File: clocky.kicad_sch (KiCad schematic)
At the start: 78 parts, among them J1 Bot 50 pin, J2 Bot 40 pin, J3 Top 50 pin, J4 Top 40 pin, J5 Power, J51 Program, J6 JST_PH, J7 Boot, Q1 AO3401A, U1 HEF4094B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

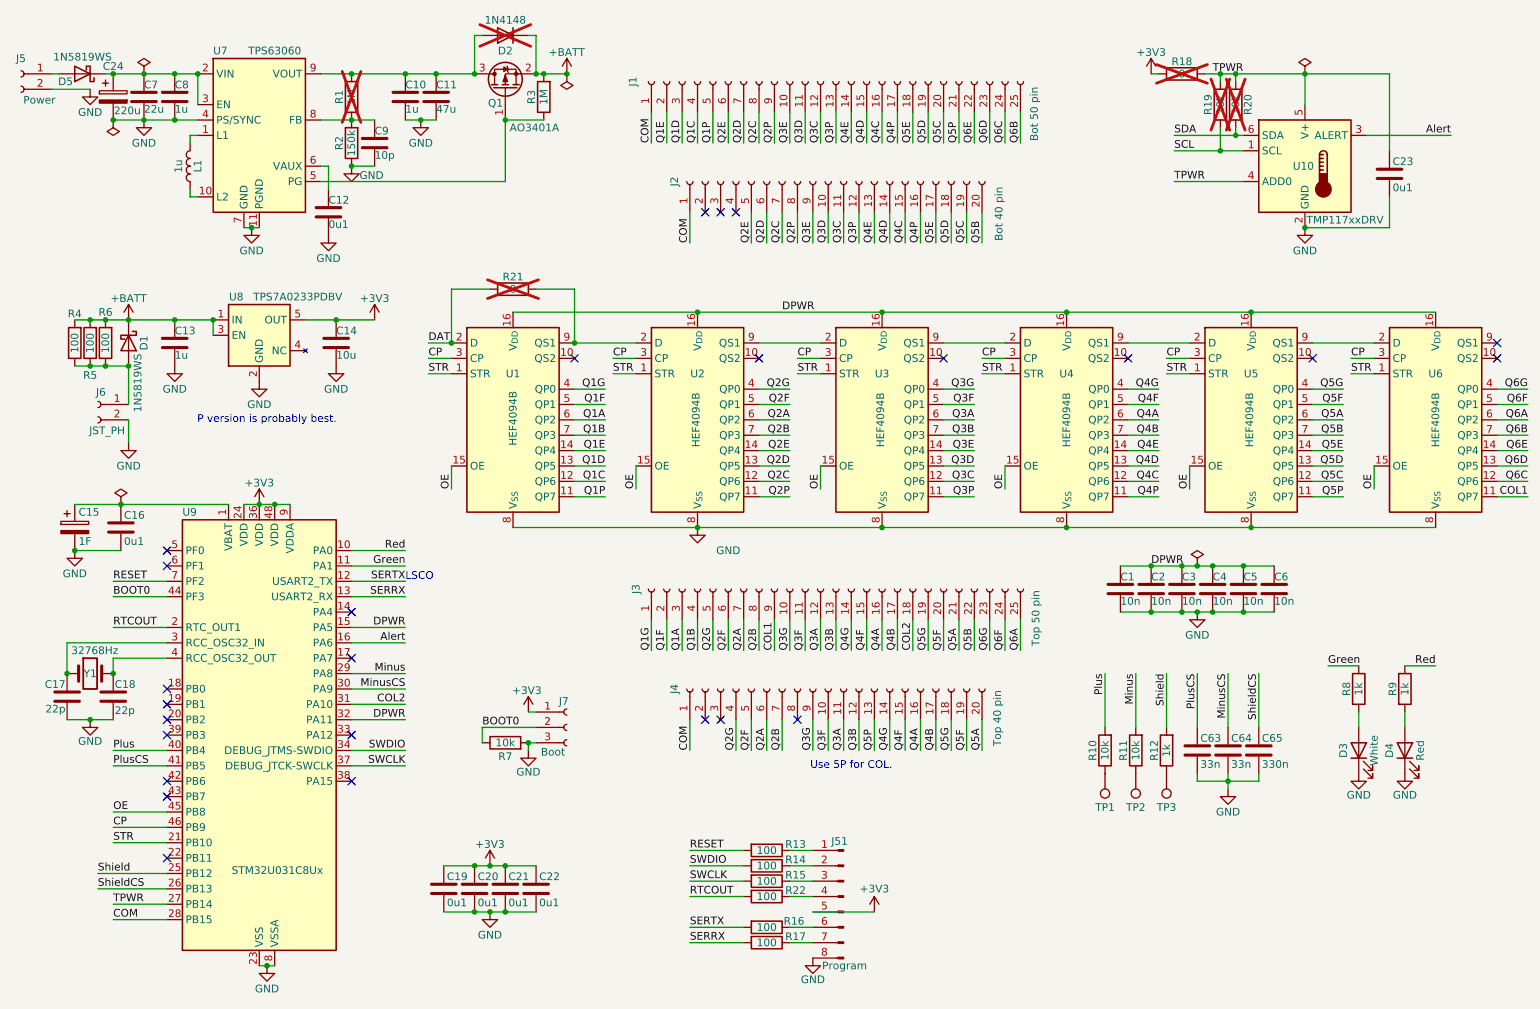
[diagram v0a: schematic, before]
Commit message: Second board layout routed.
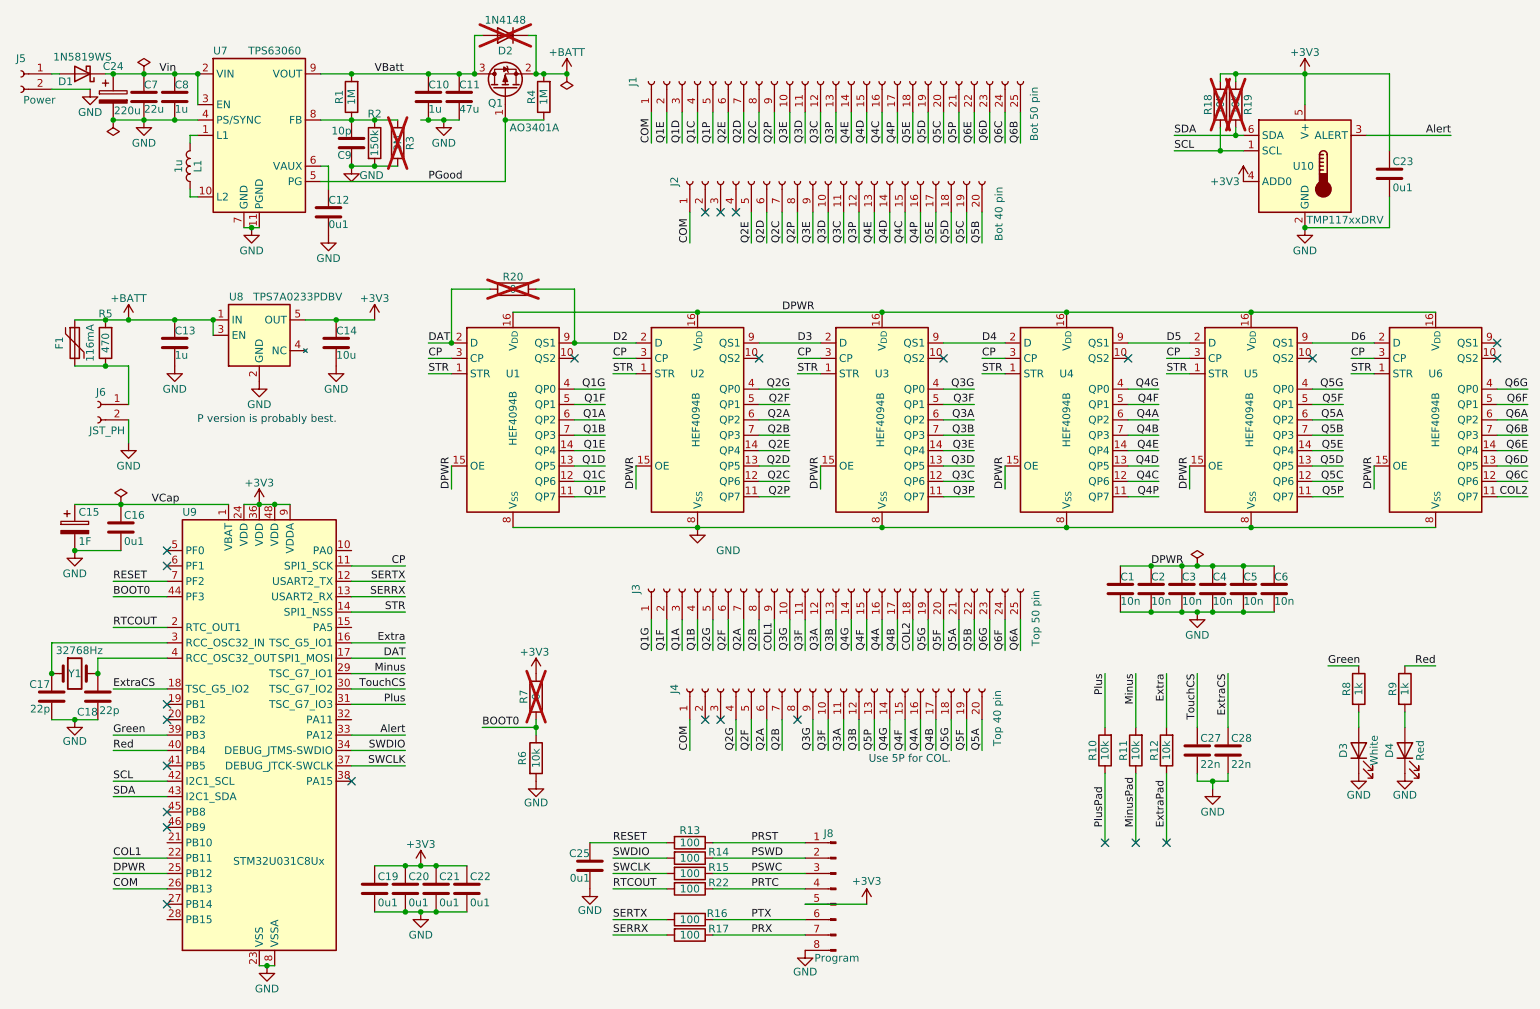
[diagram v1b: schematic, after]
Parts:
- removed C63: 33n, Capacitor_SMD:C_0603_1608Metric, symbol Device:C
- removed D1: 1N5819WS, Diode_SMD:D_SOD-323, symbol Diode:1N5819WS
- removed J7: Boot, Connector_PinSocket_2.54mm:PinSocket_1x03_P2.54mm_Vertical, symbol Connector:Conn_01x03_Socket
- removed R18: 0, symbol Device:R
- removed R4, R6: 100, Resistor_SMD:R_0603_1608Metric, symbol Device:R
- removed TP1, TP2, TP3: TestPoint, symbol Connector:TestPoint
- added C25: 0u1, Capacitor_SMD:C_0402_1005Metric, symbol Device:C
- added F1: 116mA, Resistor_SMD:R_0805_2012Metric_Pad1.20x1.40mm_HandSolder, symbol Device:Polyfuse
- added R3: 3M, Resistor_SMD:R_0603_1608Metric, symbol Device:R
- added R7: 0, Resistor_SMD:R_0603_1608Metric, symbol Device:R
- C15: footprint Capacitor_THT:C_Radial_D6.3mm_H11.0mm_P2.50mm -> Capacitor_THT:C_Radial_D8.0mm_H11.5mm_P3.50mm
- C27: renamed from C64; value 33n -> 22n; footprint Capacitor_SMD:C_0603_1608Metric -> Capacitor_SMD:C_0402_1005Metric; JLCPCB C21117 -> C1532
- C28: renamed from C65; value 330n -> 22n; footprint Capacitor_SMD:C_0603_1608Metric -> Capacitor_SMD:C_0402_1005Metric; JLCPCB C1615 -> C1532
- J1, J3: footprint Connector_PinSocket_2.54mm:PinSocket_1x25_P2.54mm_Vertical -> Parts:PinHeader_1x25_P2.54mm_Vertical
- J2, J4: footprint Connector_PinSocket_2.54mm:PinSocket_1x20_P2.54mm_Vertical -> Parts:PinSocket_1x20_P2.54mm_Vertical
- J8: renamed from J51; footprint Connector_PinHeader_2.54mm:PinHeader_1x08_P2.54mm_Vertical -> Parts:PinHeader_1x08_P2.54mm_Vertical
- Q1: JLCPCB (none) -> C15127
- R1: footprint Resistor_SMD:R_0603_1608Metric -> Resistor_SMD:R_0402_1005Metric; JLCPCB (none) -> C26083; now fitted
- R12: value 1k -> 10k; JLCPCB C11702 -> C25744
- R2: footprint Resistor_SMD:R_0603_1608Metric -> Resistor_SMD:R_0402_1005Metric; JLCPCB C22807 -> C25775
- R20: renamed from R21; footprint (none) -> Resistor_SMD:R_0603_1608Metric; now left out of the parts list
- R5: value 100 -> 470; footprint Resistor_SMD:R_0603_1608Metric -> Resistor_SMD:R_0402_1005Metric; JLCPCB C2275 -> C25117
- U1, U2, U3, U4, U5, U6: footprint Package_SO:SOIC-14_3.9x8.7mm_P1.27mm -> Package_SO:SOIC-16_3.9x9.9mm_P1.27mm
- U10: footprint Package_SON:WSON-6-1EP_2x2mm_P0.65mm_EP1x1.6mm -> Parts:WSON-6-1EP_2x2mm_P0.65mm_NoEP; JLCPCB (none) -> C699536
- U7: JLCPCB (none) -> C48567
- U8: JLCPCB (none) -> C2887324
- U9: now left out of the parts list
- renumbered D5 to D1, R19 to R18, R20 to R19, R3 to R4, R7 to R6
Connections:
- net +3V3: now also C23.1, R18.2, R19.2, U10.4 (ADD0), U10.5 (V+), R7.2
- net +BATT: now also F1.1
- net Alert: now also U9.33 (PA12); no longer U9.16 (PA6)
- net BOOT0: now also R7.1
- net COL1: now also U9.22 (PB11); no longer U6.11 (QP7)
- net COL2: now also U6.11 (QP7); no longer U9.31 (PA10)
- net COM: now also U9.26 (PB13); no longer U9.28 (PB15)
- net CP: now also U9.11 (PA1); no longer U9.46 (PB9)
- net DAT: now also U9.17 (PA7)
- net DPWR: now also U1.15 (OE), U2.15 (OE), U3.15 (OE), U4.15 (OE), U5.15 (OE), U6.15 (OE), U9.25 (PB12); no longer U9.15 (PA5), U9.32 (PA11)
- net GND: now also C9.1, R2.2, C25.2, R3.2; no longer C9.2, R2.1
- net Green: now also U9.39 (PB3); no longer U9.11 (PA1)
- net Plus: now also U9.31 (PA10); no longer U9.40 (PB4)
- net RESET: now also C25.1
- net Red: now also U9.40 (PB4); no longer U9.10 (PA0)
- net SCL: now also U9.42 (PB6)
- net SDA: now also U9.43 (PB7)
- net STR: now also U9.14 (PA4); no longer U9.21 (PB10)
- net at J6.1 (Pin_1), R5.1: now also F1.2
- net D3: now reaches U2.9 (QS1), U3.2 (D)
- net D4: now reaches U3.9 (QS1), U4.2 (D)
- net PlusPad: now reaches R10.1
- net VCap: now reaches C15.1, C16.1, U9.1 (VBAT)
- net ExtraCS: now reaches U9.18 (PB0)
- net ExtraCS: now also C28.1
- net ExtraPad: now reaches R12.1
- net D5: now reaches U4.9 (QS1), U5.2 (D)
- net D6: now reaches U5.9 (QS1), U6.2 (D)
- net Vin: now reaches C24.1, C7.1, C8.1, D1.1 (K), U7.2 (VIN), U7.3 (EN)
- net D2: now reaches R20.2, U1.9 (QS1), U2.2 (D)
- net at R1.1, U7.8 (FB): now also C9.2, R2.1, R3.1; no longer C9.1, R2.2
- net PSWC: now reaches J8.3 (Pin_3), R15.1
- net PRST: now reaches J8.1 (Pin_1), R13.1
- net VBatt: now reaches C10.1, C11.1, D2.2 (A), Q1.3 (D), R1.2, U7.9 (VOUT)
- net PRX: now reaches J8.7 (Pin_7), R17.1
- net PRTC: now reaches J8.4 (Pin_4), R22.1
- net PTX: now reaches J8.6 (Pin_6), R16.1
- net PSWD: now reaches J8.2 (Pin_2), R14.1
- net PGood: now reaches Q1.1 (G), R4.1, U7.5 (PG)
- net MinusPad: now reaches R11.1
- net MinusCS renamed TouchCS
- removed net OE: U1.15 (OE), U2.15 (OE), U3.15 (OE), U4.15 (OE), U5.15 (OE), U6.15 (OE), U9.45 (PB8)
- net PlusCS: no longer names the net of U9.41 (PB5)
- net Shield renamed Extra
- net Extra: now also U9.16 (PA6); no longer U9.25 (PB12)
- removed net ShieldCS: C28.1, U9.26 (PB13)
- removed net TPWR: C23.1, R18.2, R19.2, U10.4 (ADD0), U10.5 (V+), U9.27 (PB14)
- no-connect marks 26 -> 25
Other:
- note removed: "LSCO"
- moved on the sheet: C10, C11, C17, C18, C19, C20, C21, C22, C27, C28, C9, J8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

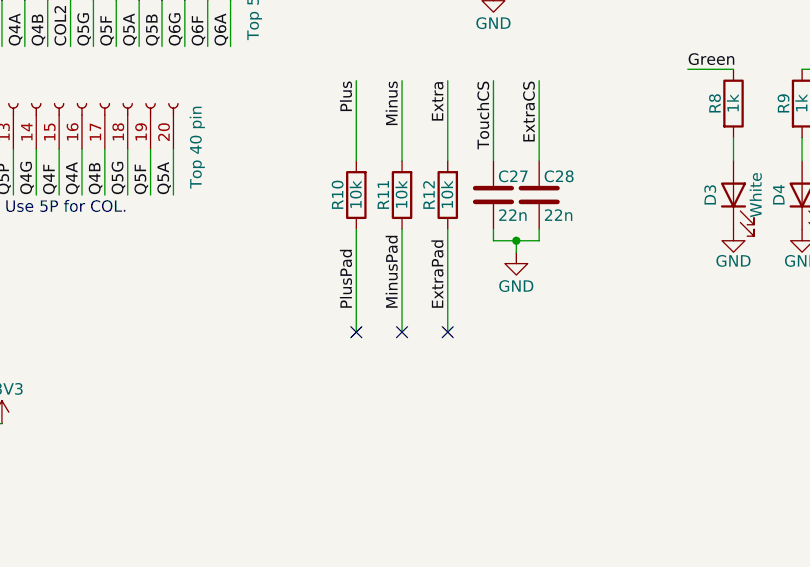
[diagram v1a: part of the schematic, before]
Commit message: DRC passes.
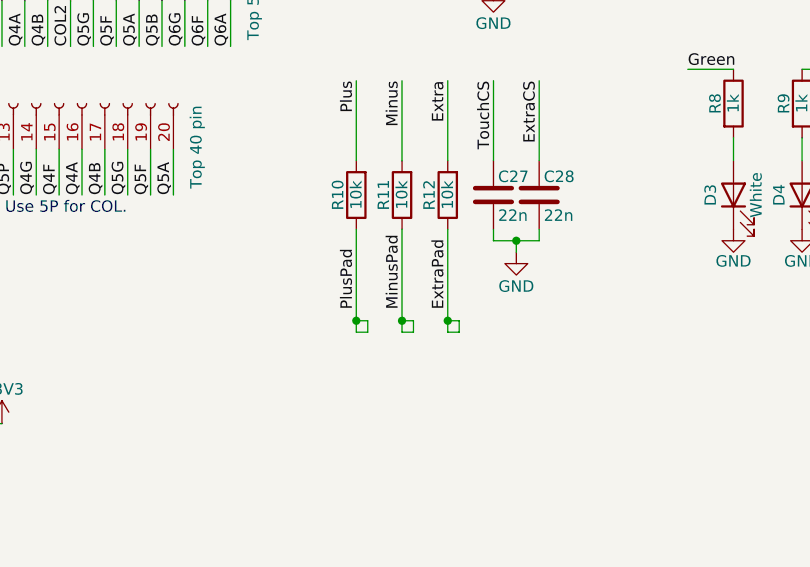
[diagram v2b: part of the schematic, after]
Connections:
- no-connect marks 25 -> 22
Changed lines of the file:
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@@
 	)
 	(junction
+		(at 209.55 156.21)
+		(diameter 0)
+		(color 0 0 0 0)
+	)
+	(junction
 		(at 222.25 147.32)
 		(diameter 0)
@@
 	)
 	(junction
+		(at 204.47 156.21)
+		(diameter 0)
+		(color 0 0 0 0)
+	)
+	(junction
 		(at 226.06 40.64)
 		(diameter 0)
@@
 	)
 	(junction
+		(at 214.63 156.21)
+		(diameter 0)
+		(color 0 0 0 0)
+	)
+	(junction
 		(at 43.18 71.12)
 		(diameter 0)
@@
 	)
 	(no_connect
-		(at 209.55 157.48)
-	)
-	(no_connect
-		(at 214.63 157.48)
-	)
-	(no_connect
 		(at 238.76 77.47)
 	)
@@
 	)
 	(no_connect
-		(at 204.47 157.48)
-	)
-	(no_connect
 		(at 153.67 137.16)
 	)
@@
 	(wire
 		(pts
-			(xy 214.63 146.05) (xy 214.63 157.48)
+			(xy 214.63 146.05) (xy 214.63 156.21)
 		)
 		(stroke
@@
 	(wire
 		(pts
+			(xy 214.63 157.48) (xy 215.9 157.48)
+		)
+		(stroke
+			(width 0)
+			(type default)
+		)
+	)
+	(wire
+		(pts
 			(xy 95.25 38.1) (xy 92.71 38.1)
 		)
@@
 	(wire
 		(pts
+			(xy 204.47 156.21) (xy 204.47 157.48)
+		)
+		(stroke
+			(width 0)
+			(type default)
+		)
+	)
+	(wire
+		(pts
 			(xy 247.65 40.64) (xy 261.62 40.64)
 		)
@@
 	(wire
 		(pts
+			(xy 204.47 157.48) (xy 205.74 157.48)
+		)
+		(stroke
+			(width 0)
+			(type default)
+		)
+	)
+	(wire
+		(pts
 			(xy 148.59 53.34) (xy 148.59 58.42)
 		)
@@
 	(wire
 		(pts
+			(xy 215.9 156.21) (xy 214.63 156.21)
+		)
+		(stroke
+			(width 0)
+			(type default)
+		)
+	)
+	(wire
+		(pts
 			(xy 116.84 100.33) (xy 121.92 100.33)
 		)
@@
 	(wire
 		(pts
+			(xy 205.74 157.48) (xy 205.74 156.21)
+		)
+		(stroke
+			(width 0)
+			(type default)
+		)
+	)
+	(wire
+		(pts
 			(xy 92.71 80.01) (xy 96.52 80.01)
 		)
@@
 	(wire
 		(pts
-			(xy 209.55 146.05) (xy 209.55 157.48)
+			(xy 209.55 146.05) (xy 209.55 156.21)
 		)
 		(stroke
@@
 	(wire
 		(pts
+			(xy 205.74 156.21) (xy 204.47 156.21)
+		)
+		(stroke
+			(width 0)
+			(type default)
+		)
+	)
+	(wire
+		(pts
 			(xy 43.18 78.74) (xy 43.18 85.09)
 		)
@@
 	(wire
 		(pts
+			(xy 214.63 156.21) (xy 214.63 157.48)
+		)
+		(stroke
+			(width 0)
+			(type default)
+		)
+	)
+	(wire
+		(pts
 			(xy 123.19 77.47) (xy 127 77.47)
 		)
@@
 	(wire
 		(pts
+			(xy 210.82 157.48) (xy 210.82 156.21)
+		)
+		(stroke
+			(width 0)
+			(type default)
+		)
+	)
+	(wire
+		(pts
 			(xy 147.32 36.83) (xy 147.32 41.91)
 		)
@@
 	(wire
 		(pts
+			(xy 209.55 156.21) (xy 209.55 157.48)
+		)
+		(stroke
+			(width 0)
+			(type default)
+		)
+	)
+	(wire
+		(pts
+			(xy 210.82 156.21) (xy 209.55 156.21)
+		)
+		(stroke
+			(width 0)
+			(type default)
+		)
+	)
+	(wire
+		(pts
 			(xy 80.01 142.24) (xy 88.9 142.24)
 		)
@@
 	(wire
 		(pts
-			(xy 204.47 146.05) (xy 204.47 157.48)
+			(xy 204.47 146.05) (xy 204.47 156.21)
 		)
 		(stroke
@@
 	(wire
 		(pts
+			(xy 209.55 157.48) (xy 210.82 157.48)
+		)
+		(stroke
+			(width 0)
+			(type default)
+		)
+	)
+	(wire
+		(pts
 			(xy 251.46 50.8) (xy 251.46 55.88)
 		)
@@
 		)
 		(stroke
+			(width 0)
+			(type default)
+		)
+	)
+	(wire
+		(pts
+			(xy 215.9 157.48) (xy 215.9 156.21)
+		)
+		(stroke

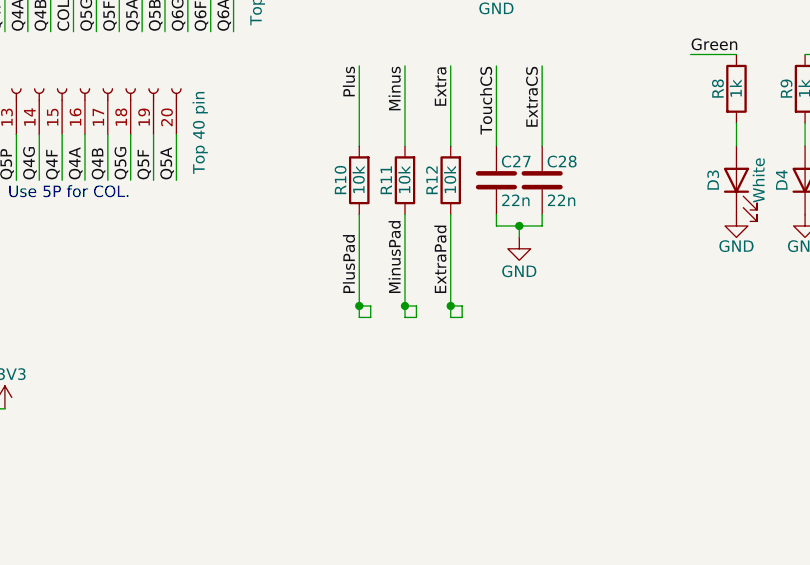
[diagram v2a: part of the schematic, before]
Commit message: Sort the touch pads out a bit.
Zones still need work.
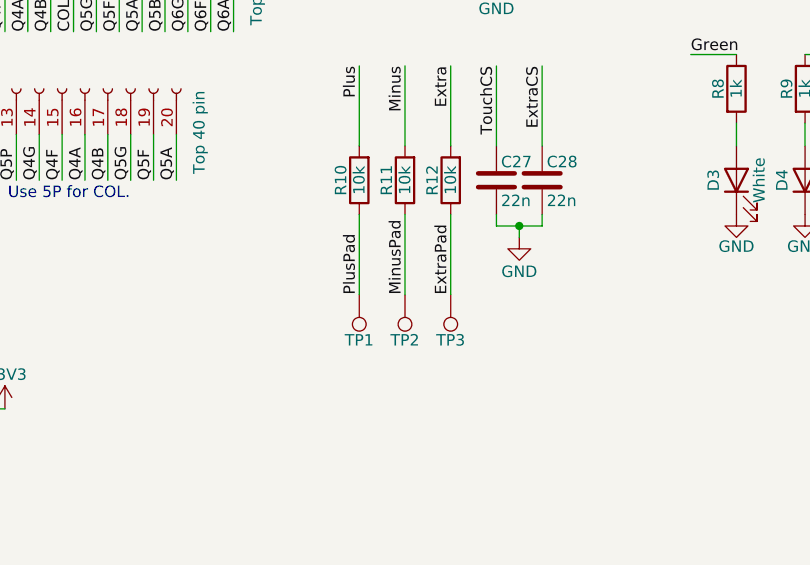
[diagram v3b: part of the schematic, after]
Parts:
- added TP1, TP2, TP3: TestPoint, Parts:Dummy, symbol Connector:TestPoint
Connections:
- net ExtraPad: now also TP3.1
- net MinusPad: now also TP2.1
- net PlusPad: now also TP1.1
